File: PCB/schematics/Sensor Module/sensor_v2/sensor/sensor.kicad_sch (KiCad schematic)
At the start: 11 parts, among them IC1 LM358DT

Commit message: Week 5 submission, with analog sensor.
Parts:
- R2, R6: footprint RESC1005X37N -> SamacSys_Parts:RESC1005X37N
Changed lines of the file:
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@@
       (effects (font (size 1.27 1.27)) (justify left))
     )
-    (property "Footprint" "RESC1005X37N" (id 2) (at 40.64 67.31 0)
+    (property "Footprint" "SamacSys_Parts:RESC1005X37N" (id 2) (at 40.64 67.31 0)
       (effects (font (size 1.27 1.27)) (justify left) hide)
     )
@@
       (effects (font (size 1.27 1.27)) (justify left))
     )
-    (property "Footprint" "RESC1005X37N" (id 2) (at 71.12 67.31 0)
+    (property "Footprint" "SamacSys_Parts:RESC1005X37N" (id 2) (at 71.12 67.31 0)
       (effects (font (size 1.27 1.27)) (justify left) hide)
     )
@@
     )
     (path "/37e3261b-9024-456f-a221-bcee5df13b69"
-      (reference "R2") (unit 1) (value "AC0402FR-07536KL") (footprint "RESC1005X37N")
+      (reference "R2") (unit 1) (value "AC0402FR-07536KL") (footprint "SamacSys_Parts:RESC1005X37N")
     )
     (path "/34f8072e-a97c-4e50-b86e-e7df6cc8f24f"
@@
     )
     (path "/f15e0257-89c9-462e-b81a-9b2f34f90520"
-      (reference "R6") (unit 1) (value "AC0402FR-07536KL") (footprint "RESC1005X37N")
-    )
-  )
+      (reference "R6") (unit 1) (value "AC0402FR-07536KL") (footprint "SamacSys_Parts:RESC1005X37N")
+    )
+  )

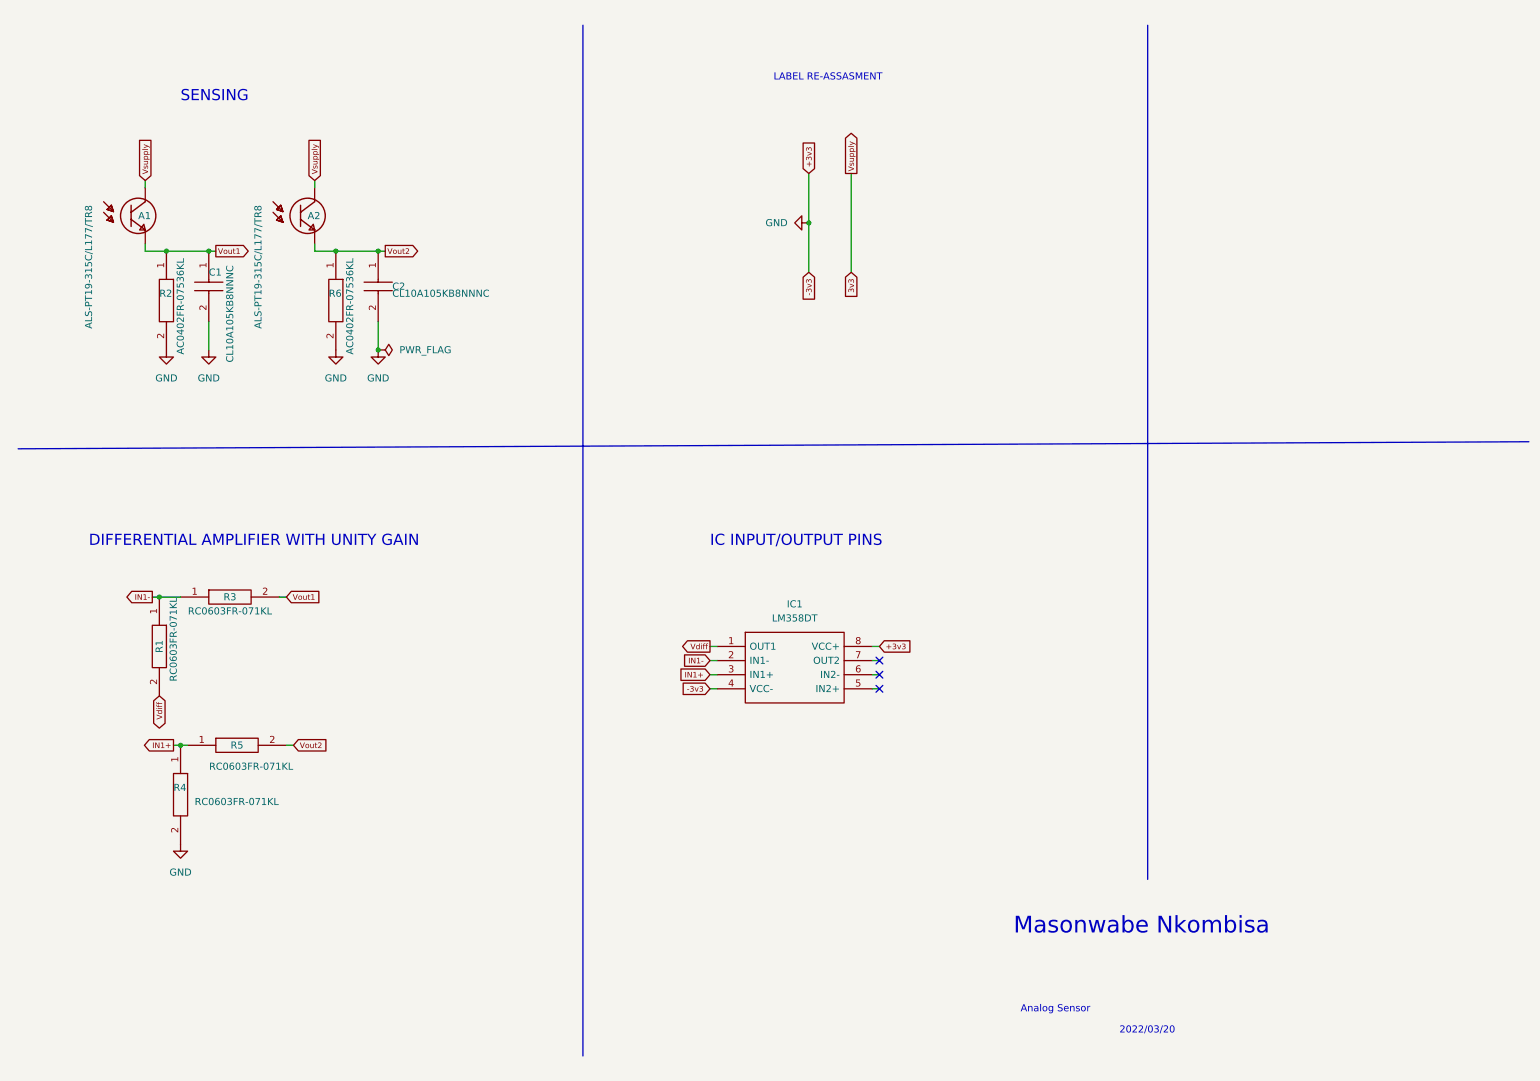
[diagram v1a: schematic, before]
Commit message: Week 5 submission, with analog sensor with pcb updated
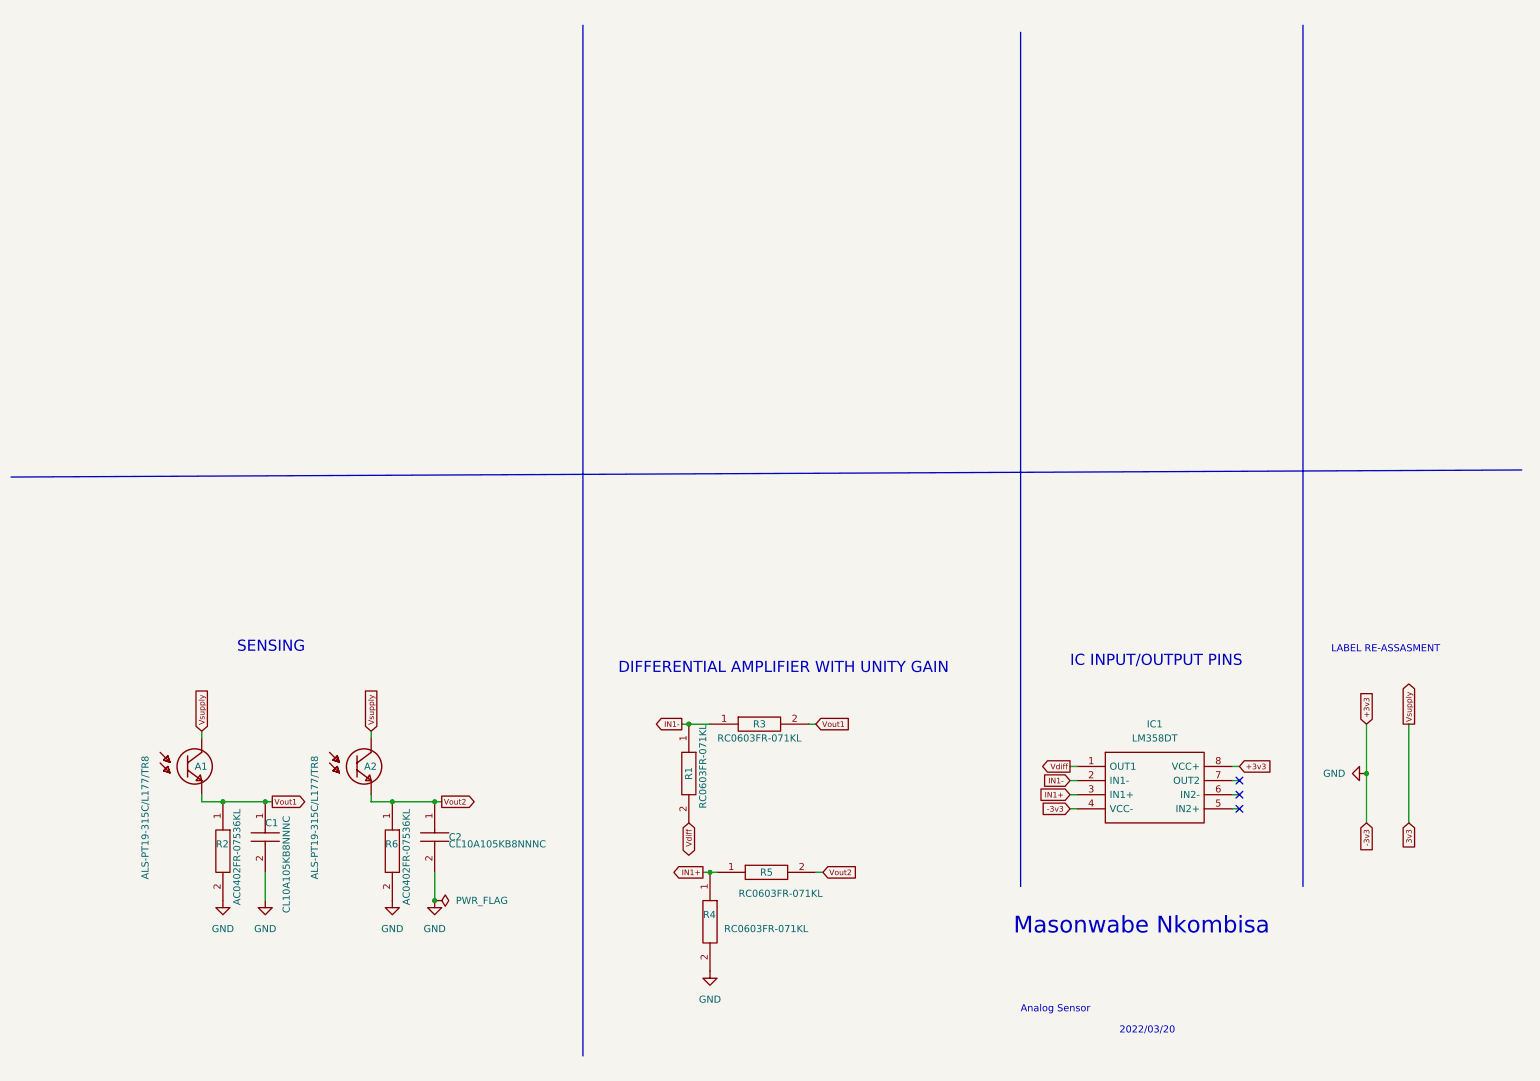
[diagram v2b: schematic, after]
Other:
- moved on the sheet: A1, A2, C1, C2, IC1, R1, R2, R3, R4, R5, R6

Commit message: Sensing module combined with main module
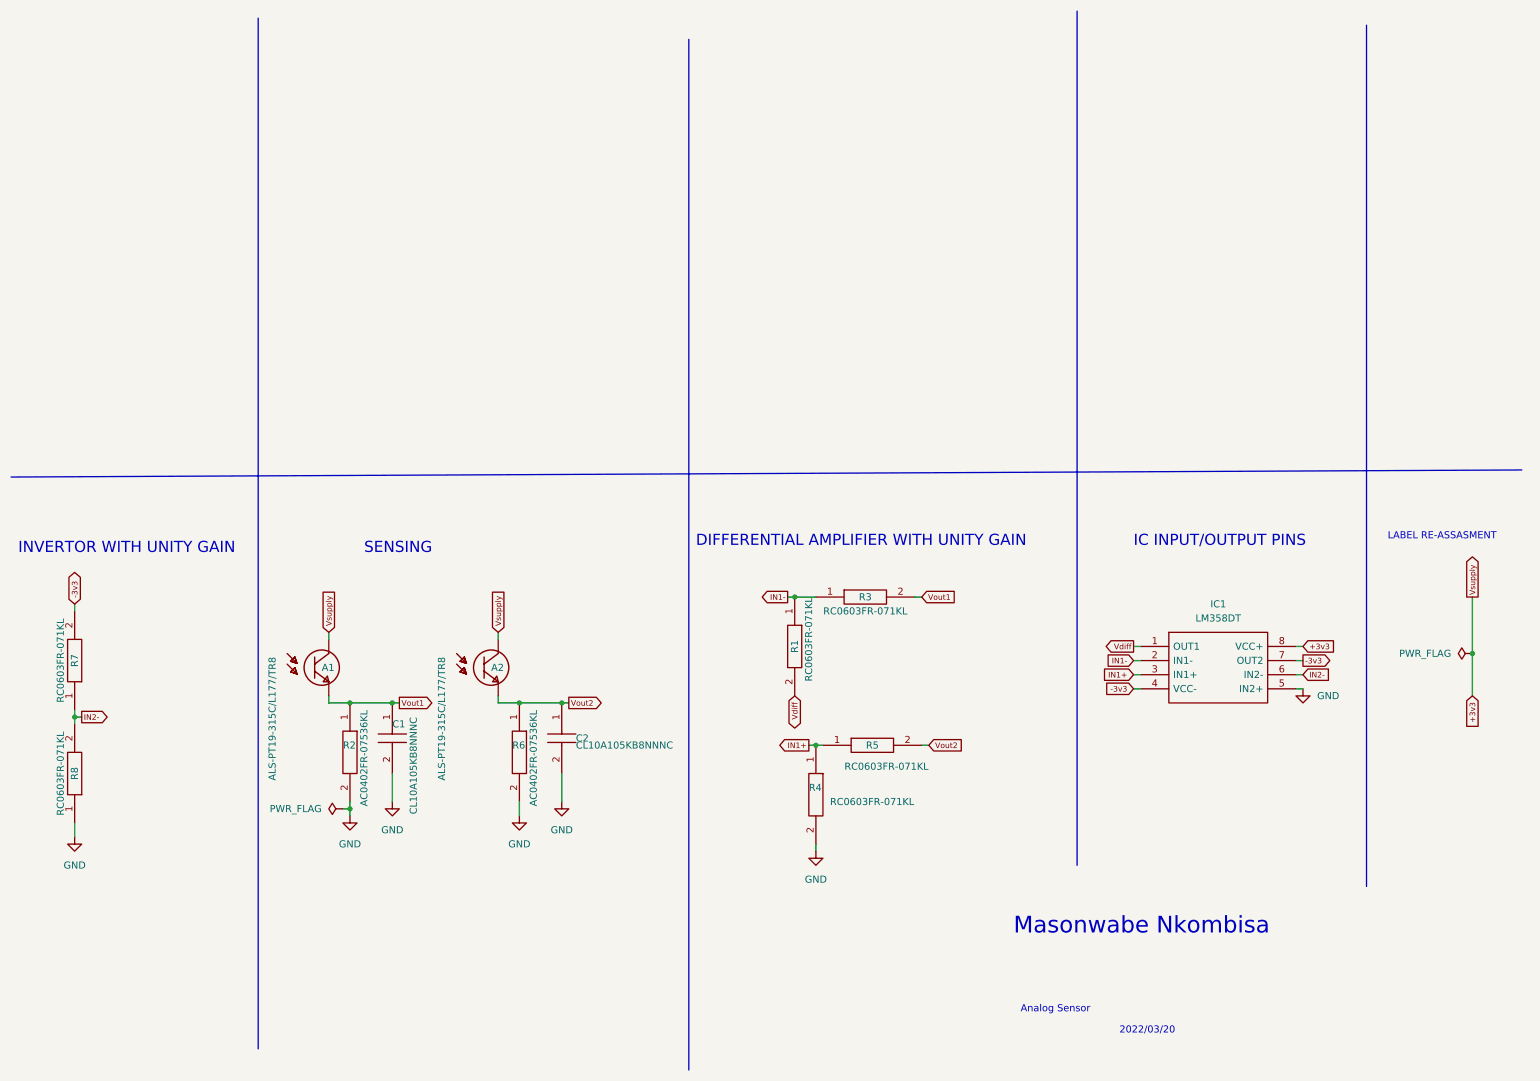
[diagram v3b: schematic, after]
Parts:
- added R7, R8: RC0603FR-071KL, SamacSys_Parts:RESC1608X55N, symbol SamacSys_Parts:RC0603FR-071KL
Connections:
- net GND: now also IC1.5 (IN2+), R8.1; no longer IC1.4 (VCC-), IC1.8 (VCC+)
- net IN2-: now reaches IC1.6 (IN2-)
- net IN2-: now also R7.1, R8.2
- net -3v3: now reaches IC1.7 (OUT2)
- net -3v3: now also IC1.4 (VCC-), R7.2
- net 3v3 renamed +3v3
- net +3v3: now also IC1.8 (VCC+)
- no-connect marks 3 -> 0
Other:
- note added: "INVERTOR WITH UNITY GAIN"
- moved on the sheet: A1, A2, C1, C2, IC1, R1, R2, R3, R4, R5, R6
